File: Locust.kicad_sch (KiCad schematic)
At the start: 0 parts

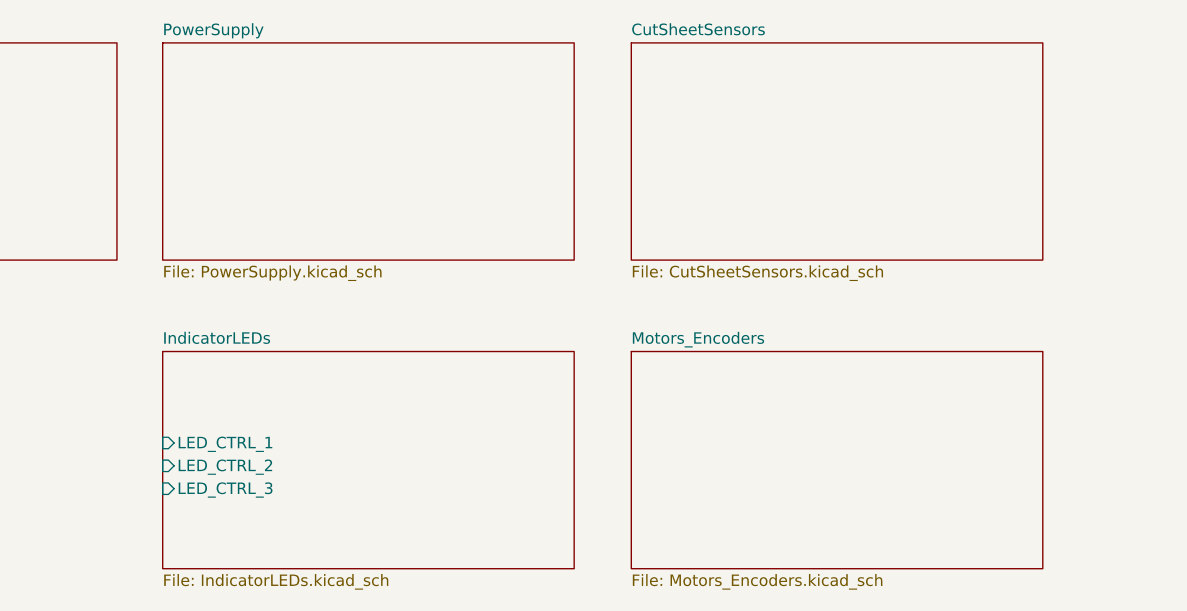
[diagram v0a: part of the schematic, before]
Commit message: Added nrf5340 and pi filters on output of switching supplies
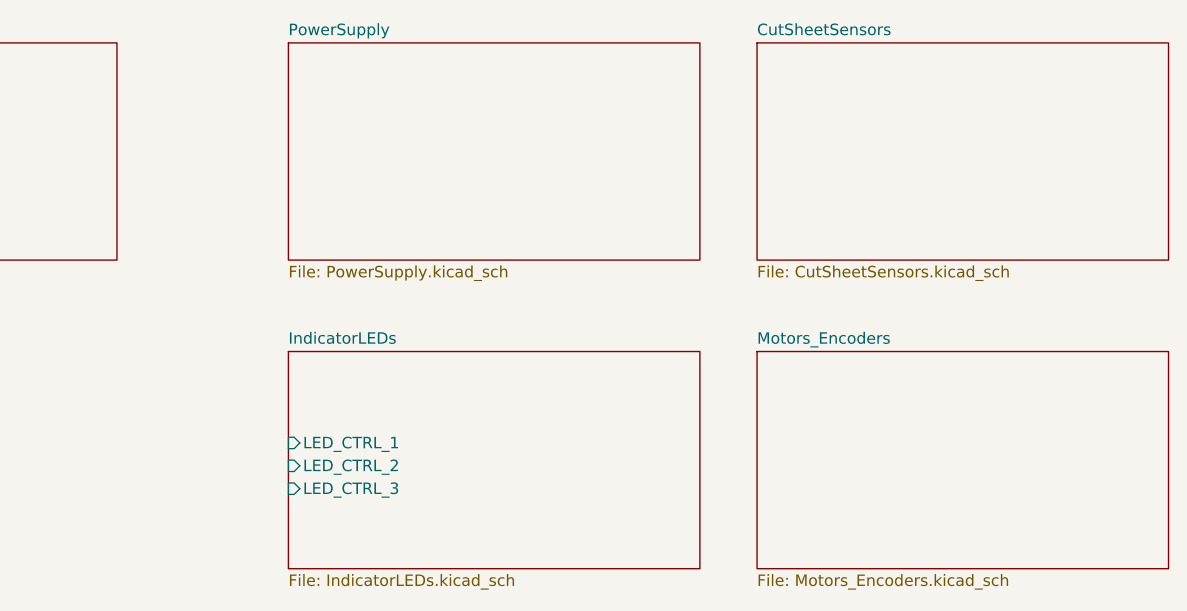
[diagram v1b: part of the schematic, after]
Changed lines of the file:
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@@
 (kicad_sch (version 20230121) (generator eeschema)
   (paper "A4")
-  (sheet (at 170.18 93.98) (size 45.72 24.13) (fields_autoplaced)
+  (sheet (at 184.15 93.98) (size 45.72 24.13) (fields_autoplaced)
     (stroke (width 0.1524) (type solid))
     (fill (color 0 0 0 0.0000))
-    (property "Sheetname" "Motors_Encoders" (at 170.18 93.2684 0)
+    (property "Sheetname" "Motors_Encoders" (at 184.15 93.2684 0)
       (effects (font (size 1.27 1.27)) (justify left bottom))
     )
-    (property "Sheetfile" "Motors_Encoders.kicad_sch" (at 170.18 118.6946 0)
+    (property "Sheetfile" "Motors_Encoders.kicad_sch" (at 184.15 118.6946 0)
       (effects (font (size 1.27 1.27)) (justify left top))
     )
     (instances
-      (project "LocustV0.1"
+      (project "Locust"
         (path "/cf97ee2f-94c3-4687-a5ea-772ffbcf72d3" (page "6"))
       )
     )
   )
-  (sheet (at 118.11 93.98) (size 45.72 24.13) (fields_autoplaced)
+  (sheet (at 132.08 93.98) (size 45.72 24.13) (fields_autoplaced)
     (stroke (width 0.1524) (type solid))
     (fill (color 0 0 0 0.0000))
-    (property "Sheetname" "IndicatorLEDs" (at 118.11 93.2684 0)
+    (property "Sheetname" "IndicatorLEDs" (at 132.08 93.2684 0)
       (effects (font (size 1.27 1.27)) (justify left bottom))
     )
-    (property "Sheetfile" "IndicatorLEDs.kicad_sch" (at 118.11 118.6946 0)
+    (property "Sheetfile" "IndicatorLEDs.kicad_sch" (at 132.08 118.6946 0)
       (effects (font (size 1.27 1.27)) (justify left top))
     )
-    (pin "LED_CTRL_3" input (at 118.11 109.22 180)
+    (pin "LED_CTRL_3" input (at 132.08 109.22 180)
       (effects (font (size 1.27 1.27)) (justify left))
     )
-    (pin "LED_CTRL_2" input (at 118.11 106.68 180)
+    (pin "LED_CTRL_2" input (at 132.08 106.68 180)
       (effects (font (size 1.27 1.27)) (justify left))
     )
-    (pin "LED_CTRL_1" input (at 118.11 104.14 180)
+    (pin "LED_CTRL_1" input (at 132.08 104.14 180)
       (effects (font (size 1.27 1.27)) (justify left))
     )
     (instances
-      (project "LocustV0.1"
+      (project "Locust"
         (path "/cf97ee2f-94c3-4687-a5ea-772ffbcf72d3" (page "5"))
       )
     )
   )
-  (sheet (at 118.11 59.69) (size 45.72 24.13) (fields_autoplaced)
+  (sheet (at 132.08 59.69) (size 45.72 24.13) (fields_autoplaced)
     (stroke (width 0.1524) (type solid))
     (fill (color 0 0 0 0.0000))
-    (property "Sheetname" "PowerSupply" (at 118.11 58.9784 0)
+    (property "Sheetname" "PowerSupply" (at 132.08 58.9784 0)
       (effects (font (size 1.27 1.27)) (justify left bottom))
     )
-    (property "Sheetfile" "PowerSupply.kicad_sch" (at 118.11 84.4046 0)
+    (property "Sheetfile" "PowerSupply.kicad_sch" (at 132.08 84.4046 0)
       (effects (font (size 1.27 1.27)) (justify left top))
     )
     (instances
-      (project "LocustV0.1"
+      (project "Locust"
         (path "/cf97ee2f-94c3-4687-a5ea-772ffbcf72d3" (page "3"))
       )
     )
   )
-  (sheet (at 170.18 59.69) (size 45.72 24.13) (fields_autoplaced)
+  (sheet (at 184.15 59.69) (size 45.72 24.13) (fields_autoplaced)
     (stroke (width 0.1524) (type solid))
     (fill (color 0 0 0 0.0000))
-    (property "Sheetname" "CutSheetSensors" (at 170.18 58.9784 0)
+    (property "Sheetname" "CutSheetSensors" (at 184.15 58.9784 0)
       (effects (font (size 1.27 1.27)) (justify left bottom))
     )
-    (property "Sheetfile" "CutSheetSensors.kicad_sch" (at 170.18 84.4046 0)
+    (property "Sheetfile" "CutSheetSensors.kicad_sch" (at 184.15 84.4046 0)
       (effects (font (size 1.27 1.27)) (justify left top))
     )
     (instances
-      (project "LocustV0.1"
+      (project "Locust"
         (path "/cf97ee2f-94c3-4687-a5ea-772ffbcf72d3" (page "4"))
       )
@@
     )
     (instances
-      (project "LocustV0.1"
+      (project "Locust"
         (path "/cf97ee2f-94c3-4687-a5ea-772ffbcf72d3" (page "2"))
       )

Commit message: 10/09/23 - Schematic v0.1
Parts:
- added H1, H2, H3, H4: MountingHole_Pad, MountingHole:MountingHole_3.7mm_Pad, symbol Mechanical:MountingHole_Pad
- added N1: Housing_Pad, symbol Mechanical:Housing_Pad
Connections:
- new net GND: H1.1, H2.1, H3.1, H4.1, N1.1 (PAD)
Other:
- sheet CutSheetSensors ports: added EDGE_DETECTOR, PHOTO_EYE_LEFT, PHOTO_EYE_RIGHT; removed none
- sheet MCU ports: added EDGE_DETECTOR, IN1_1, IN1_2/3, IN2_1, IN2_2/3, IN3_2/3, IN4_2/3, MODE_1, MODE_2/3, PHOTO_EYE_LEFT, PHOTO_EYE_RIGHT, TRQ_1, TRQ_2/3, ~{FAULT}_1, ~{FAULT}_2/3, ~{SLEEP}_1, ~{SLEEP}_2/3; removed none
- sheet Motors_Encoders ports: added IN1_1, IN1_2/3, IN2_1, IN2_2/3, IN3_2/3, IN4_2/3, MODE_1, MODE_2/3, TRQ_1, TRQ_2/3, ~{FAULT}_1, ~{FAULT}_2/3, ~{SLEEP}_1, ~{SLEEP}_2/3; removed none

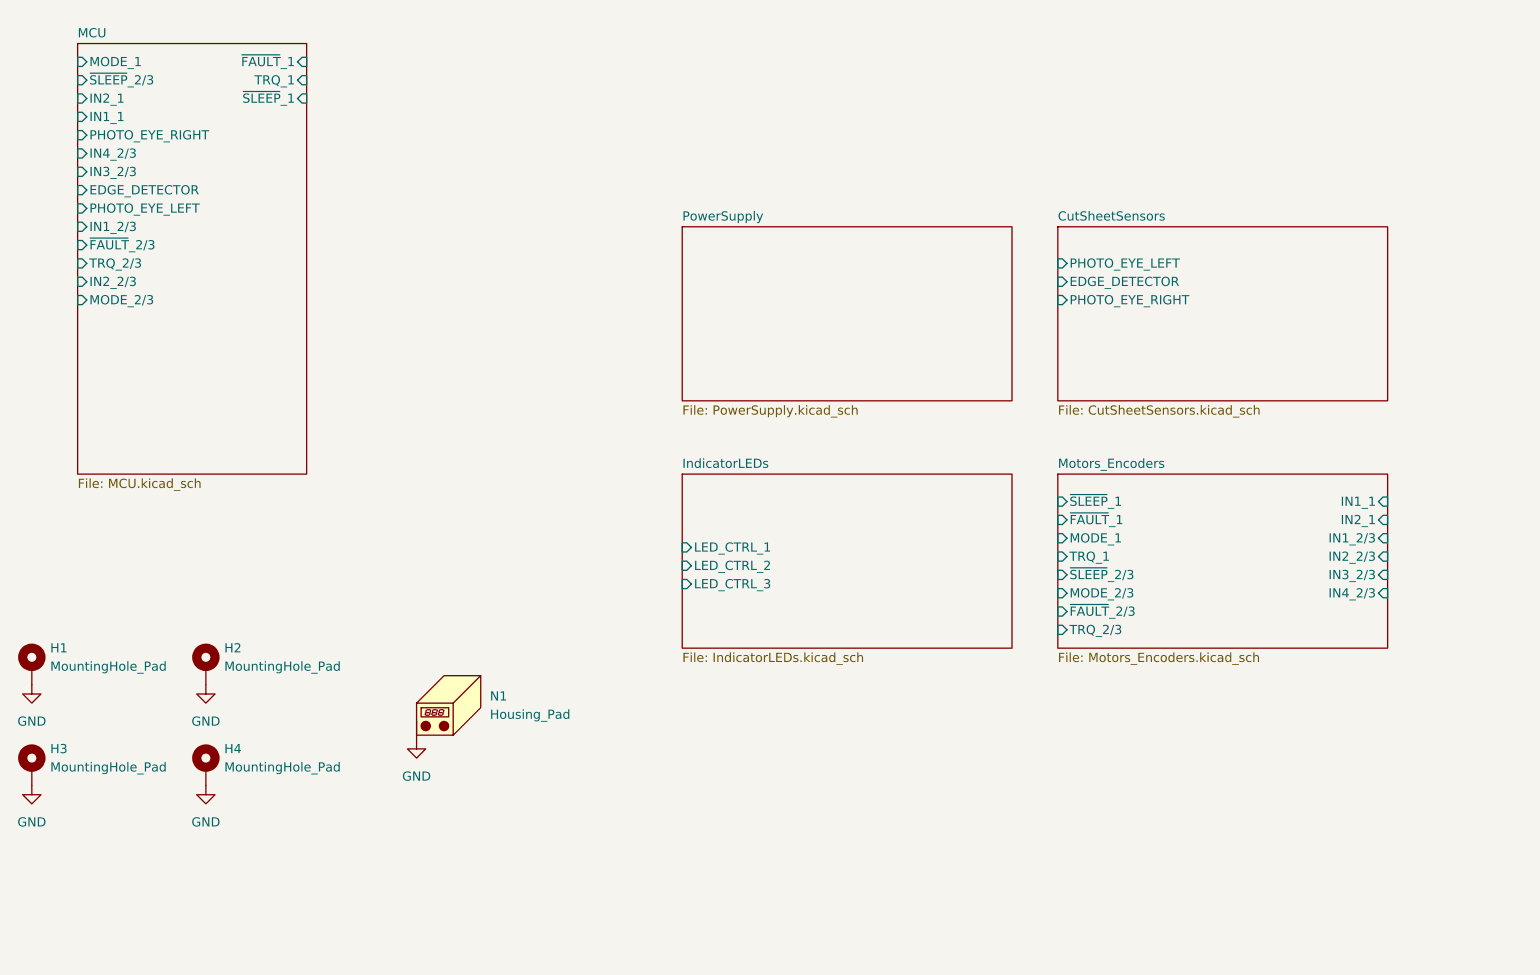
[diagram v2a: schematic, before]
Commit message: Modified README, added image, fixed schematic
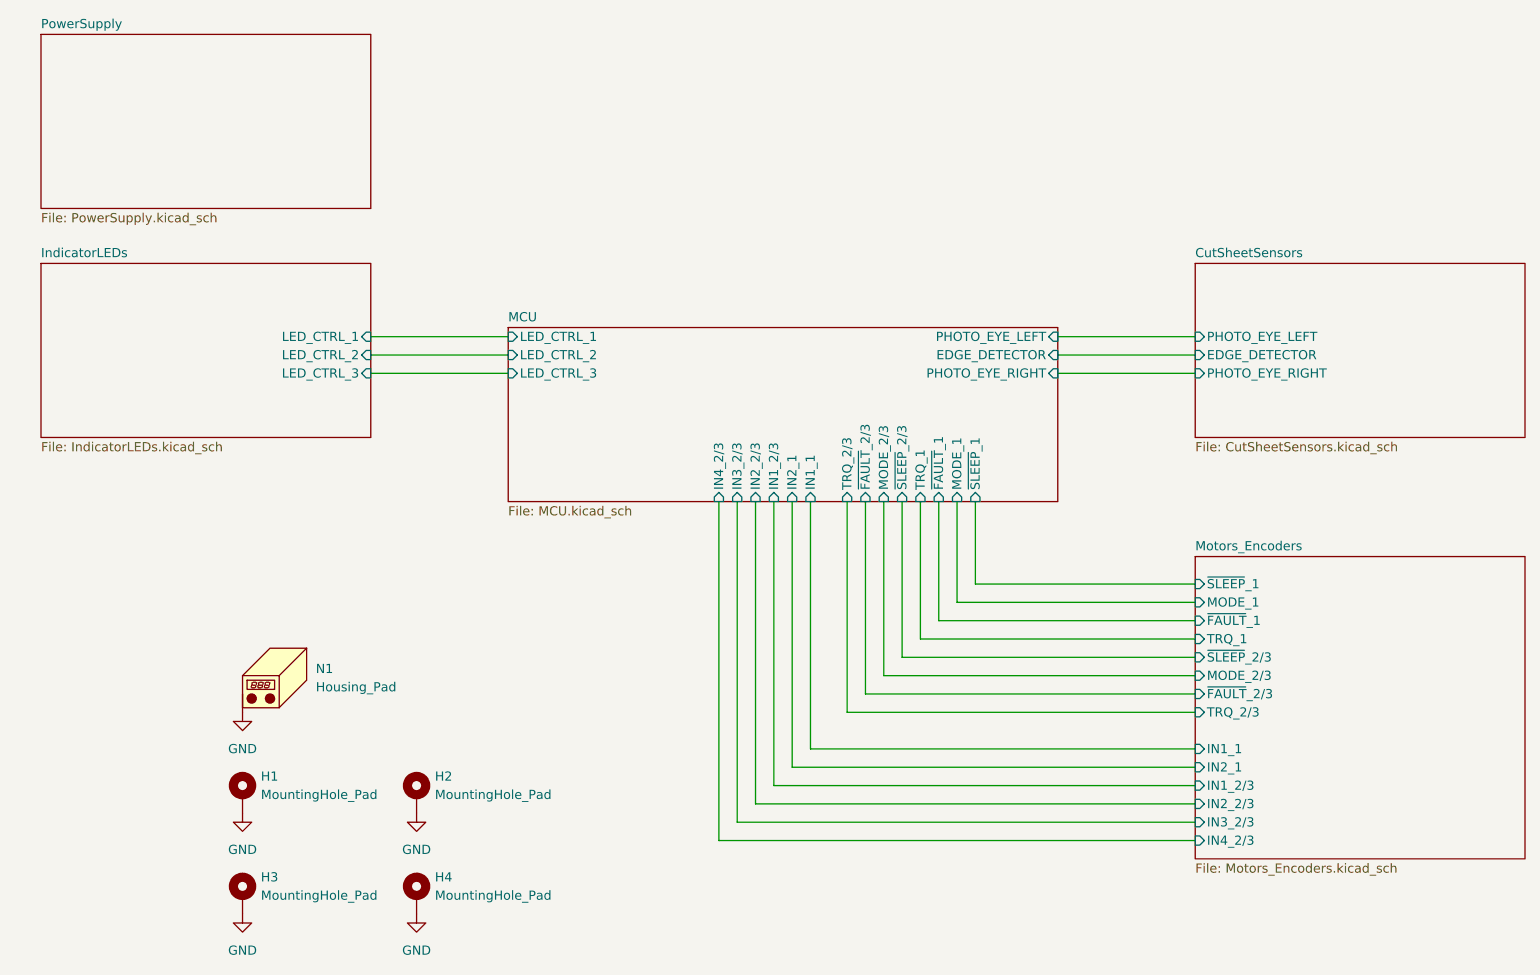
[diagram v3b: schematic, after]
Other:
- sheet MCU ports: added LED_CTRL_1, LED_CTRL_2, LED_CTRL_3; removed none
- moved on the sheet: H1, H2, H3, H4, N1
